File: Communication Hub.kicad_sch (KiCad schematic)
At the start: 50 parts, among them J1 USB_B, J2 USB_A, J3 Conn_01x03, J4 Conn_01x02, J5 RJ45, J6 RJ45, J7 RJ45, U1 USBLC6-2SC6, U2 AT24CS02-SSHM, U3 USB2514B_Bi, U4 USBLC6-2SC6, U5 CP2102N-Axx-xQFN28, U6 MAX3485, Y1 24Mhz

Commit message: Updates to schematics and pcb
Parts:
- removed C10: 1uF, Capacitor_SMD:C_0201_0603Metric, symbol Device:C
- removed C19, C20, C21: 0,1uF, Capacitor_SMD:C_0201_0603Metric, symbol Device:C
- removed R9: 10k, Resistor_SMD:R_0201_0603Metric, symbol Device:R
- removed U2: AT24CS02-SSHM, Package_SO:SOIC-8_3.9x4.9mm_P1.27mm, symbol Memory_EEPROM:AT24CS02-SSHM
- added C2: 10uF, Capacitor_SMD:C_0201_0603Metric, symbol Device:C
- added C31, C32, C36, C38, C39, C40: 0,1uF, Capacitor_SMD:C_0201_0603Metric, symbol Device:C
- added C34, C35: 4,7uF, Capacitor_SMD:C_0201_0603Metric, symbol Device:C
- added C7: 22uF, Capacitor_SMD:C_0201_0603Metric, symbol Device:C
- added J11: RS422, Connector_PinHeader_2.54mm:PinHeader_1x04_P2.54mm_Vertical, symbol Connector_Generic:Conn_01x04
- added J4: U6 TX RX, Connector_PinHeader_2.54mm:PinHeader_1x03_P2.54mm_Vertical, symbol Connector_Generic:Conn_01x03
- added J5: U7 TX RX, Connector_PinHeader_2.54mm:PinHeader_1x03_P2.54mm_Vertical, symbol Connector_Generic:Conn_01x03
- added J9: CAN, Connector_PinHeader_2.54mm:PinHeader_1x02_P2.54mm_Vertical, symbol Connector_Generic:Conn_01x02
- added R11, R12: 10k, Resistor_SMD:R_0201_0603Metric, symbol Device:R
- added R13: 49k, Resistor_SMD:R_0201_0603Metric, symbol Device:R
- added R14, R18, R19, R25, R8: 100k, Resistor_SMD:R_0201_0603Metric, symbol Device:R
- added R15, R16, R17: 235k, Resistor_SMD:R_0201_0603Metric, symbol Device:R
- added R23: 120, Resistor_SMD:R_0805_2012Metric, symbol Device:R
- added R24: `120, Resistor_SMD:R_0805_2012Metric, symbol Device:R
- added R26, R27, R28, R29: 0R, Resistor_SMD:R_0201_0603Metric, symbol Device:R
- added R5: 12k, Resistor_SMD:R_0201_0603Metric, symbol Device:R
- added S1, S2, S3, S4: PESD2CAN_215, 1_My_custom_library:DIO_PESD2CAN_215, symbol custom_symbols:PESD2CAN_215
- added U1: AMS1117-3.3, Package_TO_SOT_SMD:SOT-223-3_TabPin2, symbol Regulator_Linear:AMS1117-3.3
- added U10: MAX490E, Package_SO:SOIC-8_3.9x4.9mm_P1.27mm, symbol Interface_UART:MAX490E
- added U11, U12, U13, U8: TPS2553DBVR, 1_My_custom_library:SOT95P280X145-6N, symbol custom_symbols:TPS2553DBVR
- added U14, U15, U16, U17: TPD1E05U06DYA, Diode_SMD:D_SOD-523, symbol Power_Protection:TPD1E05U06DYA
- added U6, U7: CP2102N-Axx-xQFN28, Package_DFN_QFN:QFN-28-1EP_5x5mm_P0.5mm_EP3.35x3.35mm, symbol Interface_USB:CP2102N-Axx-xQFN28
- C10: renamed from C8; value `0,1uF -> 0,1uF
- C3: renamed from C2; value 1nF -> 1uF
- J10: renamed from J4; value Conn_01x02 -> RS485
- J3: value Conn_01x03 -> U5 TX RX; footprint Connector_PinHeader_1.00mm:PinHeader_1x03_P1.00mm_Vertical -> Connector_PinHeader_2.54mm:PinHeader_1x03_P2.54mm_Vertical
- R21: renamed from R11; footprint Resistor_SMD:R_0201_0603Metric -> Resistor_SMD:R_0805_2012Metric
- R6, R7: value 10k -> 100k
- renumbered C9 to C11, C11 to C13, C12 to C14, C13 to C15, C14 to C16, C15 to C17, C16 to C18, C17 to C19, C18 to C20, C22 to C30, C23 to C33, C24 to C37, C3 to C4, C4 to C5, C5 to C6, C6 to C8, C7 to C9, J5 to J6, J6 to J7, J7 to J8, R8 to R10, R10 to R20, R12 to R22, R5 to R9, U1 to U2, U6 to U9
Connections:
- net +3.3V: now also C31.2, C32.2, C34.2, C35.2, C7.2, R11.1, R12.1, U1.2 (VO), U6.6 (VDD), U6.7 (VREGIN), U7.6 (VDD), U7.7 (VREGIN); no longer R6.2, R7.2
- net GND: now also J3.1 (Pin_1), R6.1, R7.1, U2.5 (VBUS), U4.5 (VBUS), C2.1, C31.1, C32.1, C34.1, C35.1, C36.1, C38.1, C39.1, C40.1, C7.1, J4.3 (Pin_3), J5.1 (Pin_1), R13.2, R15.2, R16.2, R17.2, R5.1, R8.1, S1.3, S2.3, S3.3, S4.3, U1.1 (GND), U10.4 (GND), U11.2 (GND), U12.2 (GND), U13.2 (GND), U14.2 (GND), U15.2 (GND), U16.2 (GND), U17.2 (GND), U6.29 (GND), U6.3 (GND), U7.29 (GND), U7.3 (GND), U8.2 (GND); no longer J3.3 (Pin_3), U2.2 (GND), U4.2 (GND)
- net at U3.22 (SDA/SMBDATA/NON_REM1): now also R7.2; no longer R6.1
- net RS485+: now reaches J10.1 (Pin_1), R20.2, R21.1, U9.6 (A)
- net RS485+: now also J6.1, J7.1, J8.1, S3.2
- net RS485-: now reaches J10.2 (Pin_2), R21.2, R22.1, U9.7 (B)
- net RS485-: now also J6.2, J7.2, J8.2, S3.1
- net at U5.17 (RS485/GPIO.2): now also U9.2 (~{RE}), U9.3 (DE)
- net U5 RX: now reaches J3.2 (Pin_2), U5.25 (RXD), U9.1 (RO)
- net U5 RX: now also S4.2
- net U5 TX: now reaches U5.26 (TXD), U9.4 (DI)
- net U5 TX: now also J3.3 (Pin_3), S4.1; no longer J3.1 (Pin_1)
- net USD2_DP: now reaches U3.4 (USBDP_DN2/PRT_DIS_P2), U5.4 (D+)
- net USD2_DN: now reaches U3.3 (USBDM_DN2/PRT_DIS_M2), U5.5 (D-)
- net RS422 AB_P: now reaches J7.3
- net RS422 AB_P: now also J6.3, J6.4, J7.4, J8.3, J8.4, J11.4 (Pin_4), R23.1, S1.1, U10.8 (A)
- net RS422 ZY_N: now reaches J7.5
- net RS422 ZY_N: now also J6.5, J8.5, J11.2 (Pin_2), R24.1, S2.1, U10.6 (Z)
- net RS422 ZY_P: now reaches J7.6
- net RS422 ZY_P: now also J6.6, J8.6, J11.1 (Pin_1), R24.2, S2.2, U10.5 (Y)
- net CAN H: now reaches J7.7
- net CAN H: now also J6.7, J8.7, J9.2 (Pin_2)
- net CAN L: now reaches J7.8
- net CAN L: now also J6.8, J8.8, J9.1 (Pin_1)
- net USBA_DN: now reaches U4.1 (I/O1)
- net USBA_DN: now also J2.2 (D-), U3.1 (USBDM_DN1/PRT_DIS_M1), U4.6 (I/O1); no longer J2.3 (D+)
- net USBA_DP: now reaches U4.3 (I/O2)
- net USBA_DP: now also J2.3 (D+), U3.2 (USBDP_DN1/PRT_DIS_P1), U4.4 (I/O2); no longer J2.2 (D-)
- net PRTPWR1: now reaches U3.12 (PRTPWR1/BC_EN1)
- net PRTPWR1: now also U8.3 (EN)
- net OCS_N1: now reaches U3.13 (OCS_N1)
- net OCS_N1: now also R14.1, U8.4 (~{FAULT})
- net PRTPWR2: now reaches U3.16 (PRTPWR2/BC_EN2)
- net PRTPWR2: now also U13.3 (EN)
- net OCS_N2: now reaches U3.17 (OCS_N2)
- net OCS_N2: now also R25.1, U13.4 (~{FAULT})
- net PRTPWR3: now reaches U3.18 (PRTPWR3/BC_EN3)
- net PRTPWR3: now also U11.3 (EN)
- net OCS_N3: now reaches U3.19 (OCS_N3)
- net OCS_N3: now also R18.1, U11.4 (~{FAULT})
- net PRTPWR4: now reaches U3.20 (PRTPWR4/BC_EN4)
- net PRTPWR4: now also U12.3 (EN)
- net OCS_N4: now reaches U3.21 (OCS_N4)
- net OCS_N4: now also R19.1, U12.4 (~{FAULT})
- net at U3.24 (SCL/SMBCLK/CFG_SEL0): now also R6.2; no longer R7.1
- net at U3.28 (SUSP_IND/LOCAL_PWR/NON_REM0): now also R8.2
- net DN: now reaches U3.30 (USBDM_UP)
- net DN: now also J1.2 (D-), U2.1 (I/O1), U2.6 (I/O1); no longer U2.4 (I/O2)
- net DP: now reaches U3.31 (USBDP_UP)
- net DP: now also J1.3 (D+), U2.3 (I/O2), U2.4 (I/O2); no longer U2.6 (I/O1)
- net at U3.35 (RBIAS): now also R5.2
- net USD3_DN: now reaches U3.6 (USBDM_DN3/PRT_DIS_M3)
- net USD3_DN: now also U6.5 (D-)
- net USD3_DP: now reaches U3.7 (USBDP_DN3/PRT_DIS_P3)
- net USD3_DP: now also U6.4 (D+)
- net USD4_DN: now reaches U3.8 (USBDM_DN4/PRT_DIS_M4)
- net USD4_DN: now also U7.5 (D-)
- net USD4_DP: now reaches U3.9 (USBDP_DN4/PRT_DIS_P4)
- net USD4_DP: now also U7.4 (D+)
- new net: R15.1, U11.5 (ILIM)
- new net: R12.2, U7.9 (~{RST})
- new net: J2.1 (VBUS), R26.1, U4.2 (GND), U8.6 (OUT)
- new net: R13.1, U8.5 (ILIM)
- new net: R11.2, U6.9 (~{RST})
- new net: R16.1, U12.5 (ILIM)
- new net: R17.1, U13.5 (ILIM)
- new net +5V: C2.2, C3.1, C36.2, C38.2, C39.2, C40.2, J1.1 (VBUS), R14.2, R18.2, R19.2, R2.1, R25.2, R26.2, R27.2, R28.2, R29.2, U1.3 (VI), U10.1 (VCC), U11.1 (IN), U12.1 (IN), U13.1 (IN), U2.2 (GND), U8.1 (IN)
- new net RS422 AB_N: J11.3 (Pin_3), R23.2, S1.2, U10.7 (B)
- new net U6 RX: J4.2 (Pin_2), U10.2 (RO), U16.1 (I/O), U6.25 (RXD)
- new net U6 TX: J4.1 (Pin_1), U10.3 (DI), U17.1 (I/O), U6.26 (TXD)
- new net U7 RX: J5.2 (Pin_2), U15.1 (I/O), U7.25 (RXD)
- new net U7 TX: J5.3 (Pin_3), U14.1 (I/O), U7.26 (TXD)
- new net VBUS2: R27.1, U13.6 (OUT), U5.8 (VBUS)
- new net VBUS3: R28.1, U11.6 (OUT), U6.8 (VBUS)
- new net VBUS4: R29.1, U12.6 (OUT), U7.8 (VBUS)
- no-connect marks 57 -> 54
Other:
- note added: "Main"
- note added: "Outputs"
- note added: "Power"
- moved on the sheet: C1, C10, C11, C13, C14, C15, C16, C17, C18, C19, C20, C3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

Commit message: major update to pcb and corrections to schematics
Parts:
- removed C19: 0,1uF, Capacitor_SMD:C_0201_0603Metric, symbol Device:C
- removed U14, U15, U16, U17: TPD1E05U06DYA, Diode_SMD:D_SOD-523, symbol Power_Protection:TPD1E05U06DYA
- removed Y1: 24Mhz, Crystal:Crystal_HC49-4H_Vertical, symbol Device:Crystal
- added S5, S6: PESD2CAN_215, 1_My_custom_library:DIO_PESD2CAN_215, symbol custom_symbols:PESD2CAN_215
- added Y2: 24Mhz, Crystal:Crystal_SMD_5032-4Pin_5.0x3.2mm, symbol Device:Crystal_GND24
- C2, C7: footprint Capacitor_SMD:C_0201_0603Metric -> Capacitor_THT:CP_Radial_D4.0mm_P1.50mm
- R21, R23, R24: footprint Resistor_SMD:R_0805_2012Metric -> Resistor_SMD:R_0201_0603Metric
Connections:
- net GND: now also J4.1 (Pin_1), R4.1, S5.3, S6.3, Y2.2, Y2.4; no longer J4.3 (Pin_3), R4.2
- net RS422 AB_N: now also J6.4, J7.4, J8.4
- net RS422 AB_P: no longer J6.4, J7.4, J8.4
- net U6 RX: now also S5.2
- net U6 TX: now also J4.3 (Pin_3), S5.1; no longer J4.1 (Pin_1)
- net U7 RX: now also S6.2
- net U7 TX: now also S6.1
- net at R2.2, U3.27 (VBUS_DET): now also R4.2; no longer R4.1
- net at C5.2, R3.2, U3.32 (XTALOUT): now also Y2.1
- net at C4.2, R3.1, U3.33 (XTALIN/CLKIN): now also Y2.3
- net +5V renamed VBUS
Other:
- moved on the sheet: C2, C20, C30, C32, C36, C37, C38, C39, C40, J10, J11, J4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

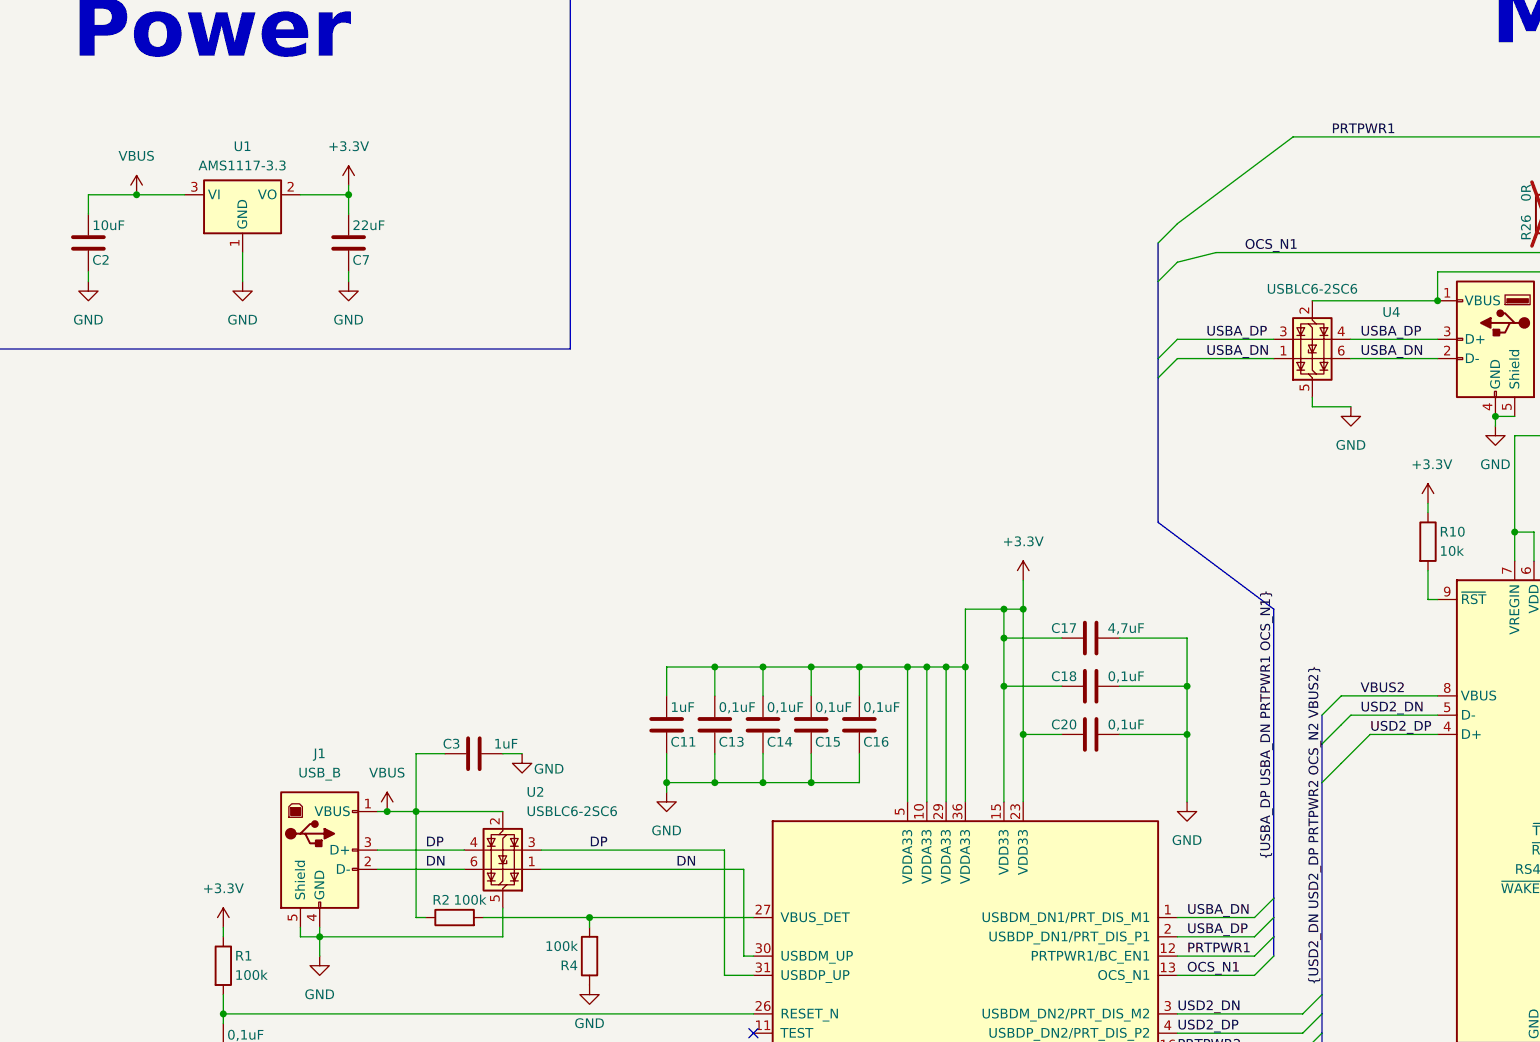
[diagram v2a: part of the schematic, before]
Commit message: Corrections to PCB (modified passive components size) Corrections to schematics(addes some capacitors and other corrections)
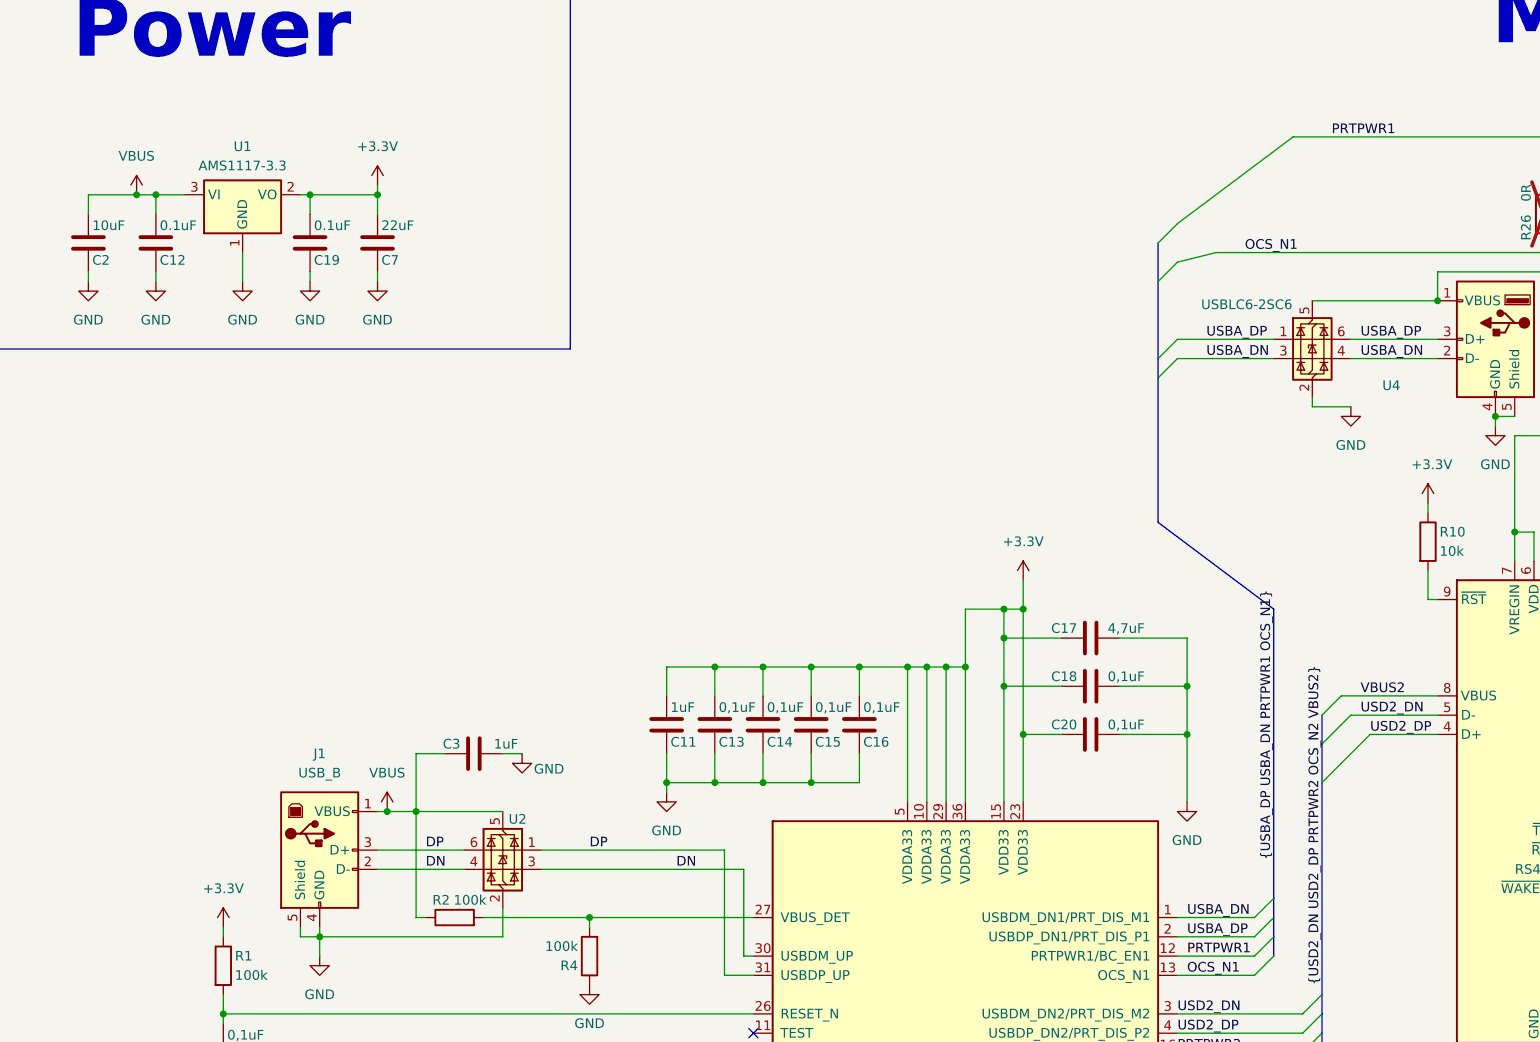
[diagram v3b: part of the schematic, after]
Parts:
- added C12, C19: 0.1uF, Capacitor_SMD:C_0603_1608Metric, symbol Device:C
- C1, C10, C11, C13, C14, C15, C16, C17, C18, C20, C3, C30, C31, C32, C33, C34, C35, C36, C37, C38, C39, C4, C40, C5, C6, C8, C9: footprint Capacitor_SMD:C_0201_0603Metric -> Capacitor_SMD:C_0603_1608Metric
- R1, R10, R11, R12, R13, R14, R15, R16, R17, R18, R19, R2, R20, R21, R22, R23, R24, R25, R26, R27, R28, R29, R3, R4, R5, R6, R7, R8, R9: footprint Resistor_SMD:R_0201_0603Metric -> Resistor_SMD:R_0603_1608Metric
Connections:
- net +3.3V: now also C19.2
- net DN: now also U2.3 (I/O2), U2.4 (I/O2); no longer U2.1 (I/O1), U2.6 (I/O1)
- net DP: now also U2.1 (I/O1), U2.6 (I/O1); no longer U2.3 (I/O2), U2.4 (I/O2)
- net GND: now also U2.2 (GND), U4.2 (GND), C12.1, C19.1; no longer U2.5 (VBUS), U4.5 (VBUS)
- net USBA_DN: now also U4.3 (I/O2), U4.4 (I/O2); no longer U4.1 (I/O1), U4.6 (I/O1)
- net USBA_DP: now also U4.1 (I/O1), U4.6 (I/O1); no longer U4.3 (I/O2), U4.4 (I/O2)
- net VBUS: now also U2.5 (VBUS), C12.2; no longer U2.2 (GND)
- net at J2.1 (VBUS), R26.1, U8.6 (OUT): now also U4.5 (VBUS); no longer U4.2 (GND)
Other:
- moved on the sheet: C7, U2

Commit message: Schematics reorganized and PCB size optimized
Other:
- note added: "3.3V 5V"
- note added: "Current limiters"
- note added: "Output pin connectors"
- note added: "RJ45 Output"
- note added: "RS422"
- note added: "RS485"
- note added: "USB A Output"
- note added: "USB UART & Drivers"
- note added: "Usb Hub"
- note removed: "Main"
- moved on the sheet: C1, C10, C11, C12, C13, C14, C15, C16, C17, C18, C19, C2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
